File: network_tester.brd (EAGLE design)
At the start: 60.6 x 69.8 mm, 47 parts, among them SW1 SPST_TACT-KMR2, U1 Joystick, U2 RN2483, U3 ATSAMD21G-A, U5 MCP1640, X1 GPS, X2 868, X3 32.768, X4 microUSB, X5 434

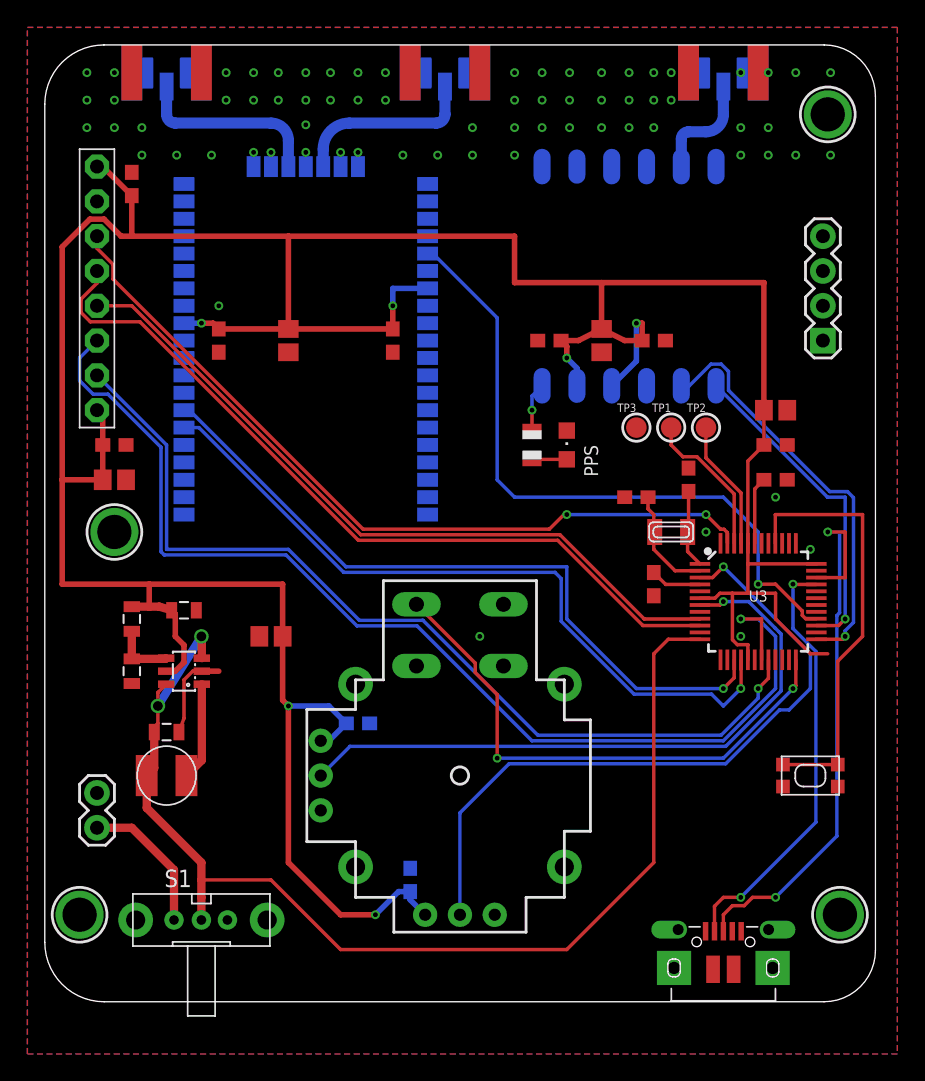
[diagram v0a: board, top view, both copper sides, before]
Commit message: Test points added, fixed board labels
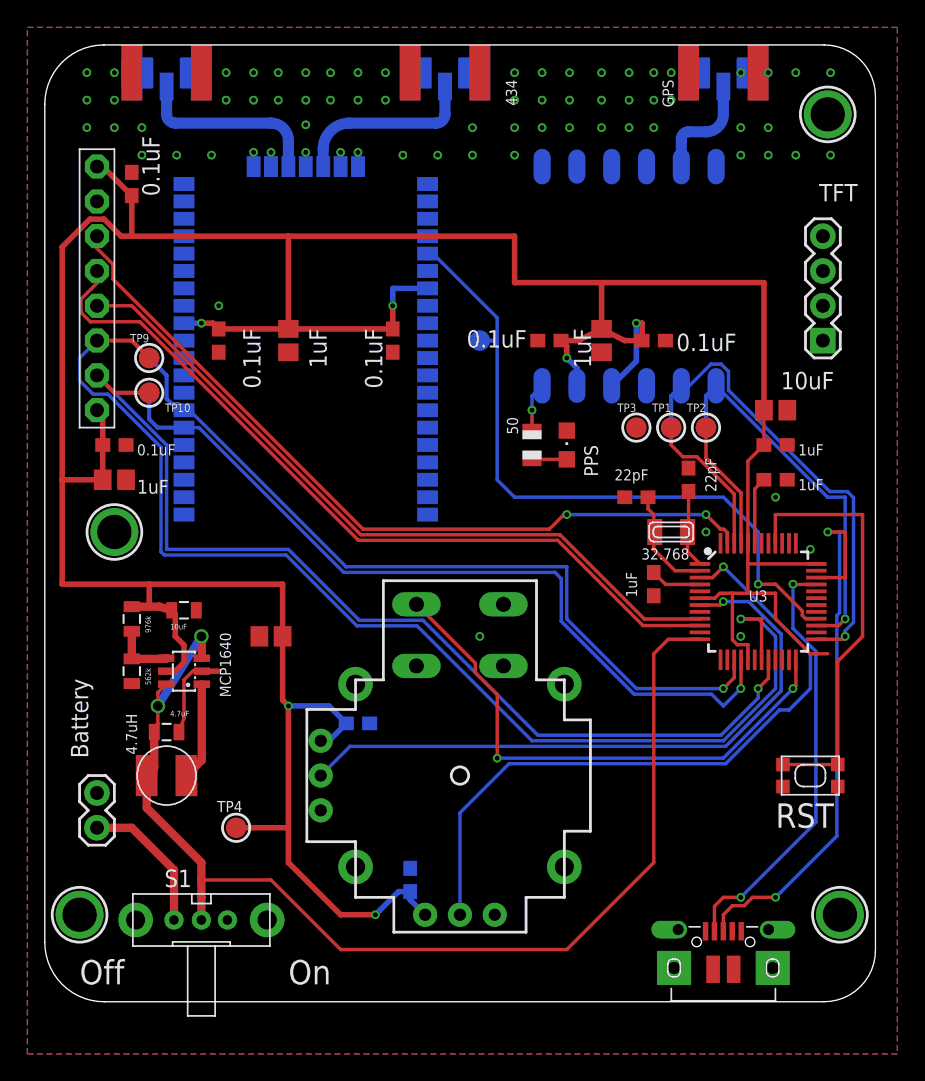
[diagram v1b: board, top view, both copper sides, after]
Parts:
- added TP10, TP14, TP4, TP5, TP6, TP7, TP8, TP9: (no value), Adafruit Feather M0 Basic rev C:TESTPOINT_ROUND_1.5MM
- C1, C12, C14, C15, C19, C2, C21, C9: value 1uF -> 0.1uF
- C16, C18, C3, C8: value 10uF -> 1uF
- R1: value 1K -> 50
- renumbered X1 to GPS, X2 to 868, X5 to 434
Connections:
- net 3V: now also TP4.P$1
- net MOSI: now also TP9.P$1
- net RN2483_RESET: now also TP14.P$1
- net SCK: now also TP10.P$1
- net UART_GPS_RX: now also TP7.P$1
- net UART_GPS_TX: now also TP8.P$1
- net UART_RN2483_RX: now also TP6.P$1
- net UART_RN2483_TX: now also TP5.P$1
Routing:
- net UART_RN2483_TX: track 52.4 -> 57.6 mm
- net UART_RN2483_RX: track 53.9 -> 58.6 mm
- net SCK: track 67.8 -> 72.2 mm
- net MOSI: track 82.6 -> 86.9 mm
- net 3V: track 257.1 -> 260.9 mm
- net UART_GPS_RX: track 30.6 -> 34.0 mm
- net UART_GPS_TX: track 24.0 -> 27.3 mm
- net RN2483_RESET: track 48.8 -> 50.0 mm
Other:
- board text added: "Off"
- board text added: "On"
- board text added: "RST"
